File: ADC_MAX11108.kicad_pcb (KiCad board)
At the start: 4 copper layers, 100 x 100 mm, 82 parts, among them IC1 MAX11108AVB+T, IC2 MAX11108AVB+T, IC22 524SDCGI8, IC24 524SDCGI8, IC26 524SDCGI8, IC28 524SDCGI8, IC30 LMS1585ACSX-ADJ_NOPB, J1 Conn_01x02_Pin, J2 Conn_01x03_Pin, J3 Conn_01x07_Pin, J4 Conn_01x07_Pin, J5 Conn_01x07_Pin, J6 Conn_01x08_Pin, J7 Conn_01x08_Pin, Q1 LMS1587CT-3.3_NOPB, U1 ADR4533, U2 ADR4533, U3 ADR4533, U4 ADR4533, U5 ADR4533

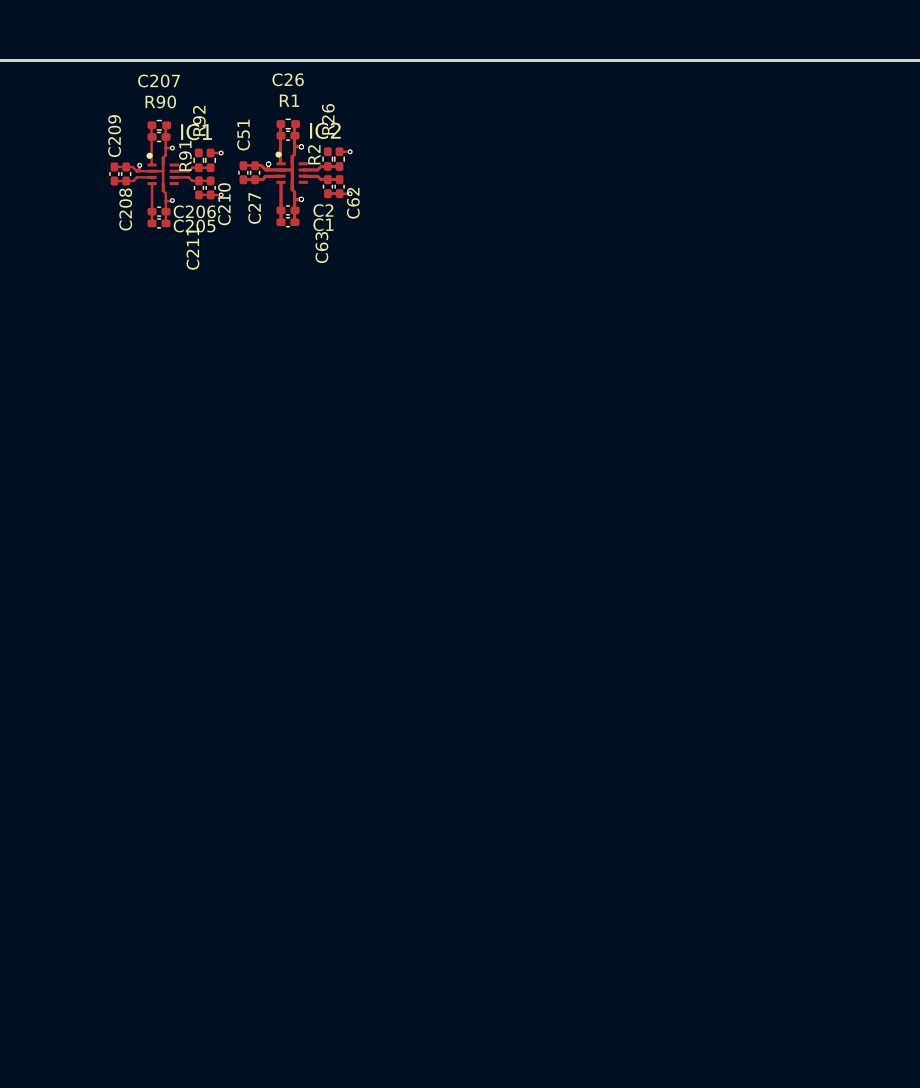
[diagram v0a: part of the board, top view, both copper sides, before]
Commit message: figured out footprint issue and replicated the 25 ADCs in the routing part as well
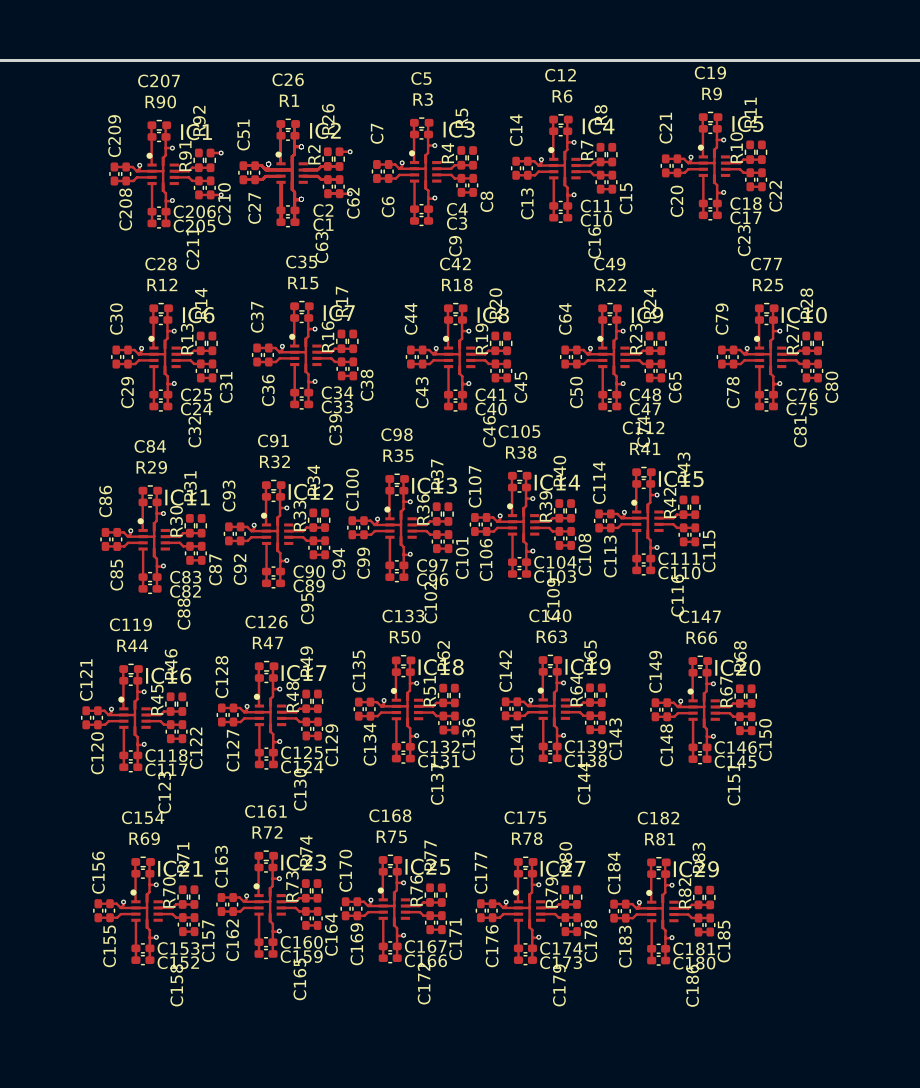
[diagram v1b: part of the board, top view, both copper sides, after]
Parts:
- added C10: 10uF, Capacitor_SMD:C_0402_1005Metric_Pad0.74x0.62mm_HandSolder, F.Cu at (148.7, 61.6)
- added C100: 10uF, Capacitor_SMD:C_0402_1005Metric_Pad0.74x0.62mm_HandSolder, F.Cu at (131.8, 86.8)
- added C101: 10uF, Capacitor_SMD:C_0402_1005Metric_Pad0.74x0.62mm_HandSolder, F.Cu at (139.6, 87.9)
- added C102: 0.1uF, Capacitor_SMD:C_0402_1005Metric_Pad0.74x0.62mm_HandSolder, F.Cu at (138.6, 87.9)
- added C103: 10uF, Capacitor_SMD:C_0402_1005Metric_Pad0.74x0.62mm_HandSolder, F.Cu at (145.3, 90.5)
- added C104: 0.1uF, Capacitor_SMD:C_0402_1005Metric_Pad0.74x0.62mm_HandSolder, F.Cu at (145.3, 89.6)
- added C105: 470pF, Capacitor_SMD:C_0402_1005Metric_Pad0.74x0.62mm_HandSolder, F.Cu at (145.3, 83.5)
- added C106: 0.1uF, Capacitor_SMD:C_0402_1005Metric_Pad0.74x0.62mm_HandSolder, F.Cu at (142.7, 86.5)
- added C107: 10uF, Capacitor_SMD:C_0402_1005Metric_Pad0.74x0.62mm_HandSolder, F.Cu at (141.7, 86.5)
- added C108: 10uF, Capacitor_SMD:C_0402_1005Metric_Pad0.74x0.62mm_HandSolder, F.Cu at (149.5, 87.6)
- added C109: 0.1uF, Capacitor_SMD:C_0402_1005Metric_Pad0.74x0.62mm_HandSolder, F.Cu at (148.6, 87.6)
- added C11: 0.1uF, Capacitor_SMD:C_0402_1005Metric_Pad0.74x0.62mm_HandSolder, F.Cu at (148.7, 60.7)
- added C110: 10uF, Capacitor_SMD:C_0402_1005Metric_Pad0.74x0.62mm_HandSolder, F.Cu at (155.4, 90.2)
- added C111: 0.1uF, Capacitor_SMD:C_0402_1005Metric_Pad0.74x0.62mm_HandSolder, F.Cu at (155.4, 89.3)
- added C112: 470pF, Capacitor_SMD:C_0402_1005Metric_Pad0.74x0.62mm_HandSolder, F.Cu at (155.4, 83.2)
- added C113: 0.1uF, Capacitor_SMD:C_0402_1005Metric_Pad0.74x0.62mm_HandSolder, F.Cu at (152.7, 86.2)
- added C114: 10uF, Capacitor_SMD:C_0402_1005Metric_Pad0.74x0.62mm_HandSolder, F.Cu at (151.8, 86.2)
- added C115: 10uF, Capacitor_SMD:C_0402_1005Metric_Pad0.74x0.62mm_HandSolder, F.Cu at (159.6, 87.3)
- added C116: 0.1uF, Capacitor_SMD:C_0402_1005Metric_Pad0.74x0.62mm_HandSolder, F.Cu at (158.6, 87.3)
- added C117: 10uF, Capacitor_SMD:C_0402_1005Metric_Pad0.74x0.62mm_HandSolder, F.Cu at (113.8, 106.2)
- added C118: 0.1uF, Capacitor_SMD:C_0402_1005Metric_Pad0.74x0.62mm_HandSolder, F.Cu at (113.8, 105.2)
- added C119: 470pF, Capacitor_SMD:C_0402_1005Metric_Pad0.74x0.62mm_HandSolder, F.Cu at (113.8, 99.2)
- added C12: 470pF, Capacitor_SMD:C_0402_1005Metric_Pad0.74x0.62mm_HandSolder, F.Cu at (148.7, 54.6)
- added C120: 0.1uF, Capacitor_SMD:C_0402_1005Metric_Pad0.74x0.62mm_HandSolder, F.Cu at (111.2, 102.2)
- added C121: 10uF, Capacitor_SMD:C_0402_1005Metric_Pad0.74x0.62mm_HandSolder, F.Cu at (110.2, 102.2)
- added C122: 10uF, Capacitor_SMD:C_0402_1005Metric_Pad0.74x0.62mm_HandSolder, F.Cu at (118.0, 103.3)
- added C123: 0.1uF, Capacitor_SMD:C_0402_1005Metric_Pad0.74x0.62mm_HandSolder, F.Cu at (117.1, 103.3)
- added C124: 10uF, Capacitor_SMD:C_0402_1005Metric_Pad0.74x0.62mm_HandSolder, F.Cu at (124.8, 105.9)
- added C125: 0.1uF, Capacitor_SMD:C_0402_1005Metric_Pad0.74x0.62mm_HandSolder, F.Cu at (124.8, 105.0)
- added C126: 470pF, Capacitor_SMD:C_0402_1005Metric_Pad0.74x0.62mm_HandSolder, F.Cu at (124.8, 98.9)
- added C127: 0.1uF, Capacitor_SMD:C_0402_1005Metric_Pad0.74x0.62mm_HandSolder, F.Cu at (122.2, 101.9)
- added C128: 10uF, Capacitor_SMD:C_0402_1005Metric_Pad0.74x0.62mm_HandSolder, F.Cu at (121.2, 101.9)
- added C129: 10uF, Capacitor_SMD:C_0402_1005Metric_Pad0.74x0.62mm_HandSolder, F.Cu at (129.0, 103.1)
- added C13: 0.1uF, Capacitor_SMD:C_0402_1005Metric_Pad0.74x0.62mm_HandSolder, F.Cu at (146.0, 57.6)
- added C130: 0.1uF, Capacitor_SMD:C_0402_1005Metric_Pad0.74x0.62mm_HandSolder, F.Cu at (128.1, 103.1)
- added C131: 10uF, Capacitor_SMD:C_0402_1005Metric_Pad0.74x0.62mm_HandSolder, F.Cu at (135.9, 105.5)
- added C132: 0.1uF, Capacitor_SMD:C_0402_1005Metric_Pad0.74x0.62mm_HandSolder, F.Cu at (135.9, 104.5)
- added C133: 470pF, Capacitor_SMD:C_0402_1005Metric_Pad0.74x0.62mm_HandSolder, F.Cu at (135.9, 98.5)
- added C134: 0.1uF, Capacitor_SMD:C_0402_1005Metric_Pad0.74x0.62mm_HandSolder, F.Cu at (133.2, 101.5)
- added C135: 10uF, Capacitor_SMD:C_0402_1005Metric_Pad0.74x0.62mm_HandSolder, F.Cu at (132.3, 101.5)
- added C136: 10uF, Capacitor_SMD:C_0402_1005Metric_Pad0.74x0.62mm_HandSolder, F.Cu at (140.1, 102.6)
- added C137: 0.1uF, Capacitor_SMD:C_0402_1005Metric_Pad0.74x0.62mm_HandSolder, F.Cu at (139.2, 102.6)
- added C138: 10uF, Capacitor_SMD:C_0402_1005Metric_Pad0.74x0.62mm_HandSolder, F.Cu at (147.8, 105.4)
- added C139: 0.1uF, Capacitor_SMD:C_0402_1005Metric_Pad0.74x0.62mm_HandSolder, F.Cu at (147.8, 104.5)
- added C14: 10uF, Capacitor_SMD:C_0402_1005Metric_Pad0.74x0.62mm_HandSolder, F.Cu at (145.1, 57.6)
- added C140: 470pF, Capacitor_SMD:C_0402_1005Metric_Pad0.74x0.62mm_HandSolder, F.Cu at (147.8, 98.4)
- added C141: 0.1uF, Capacitor_SMD:C_0402_1005Metric_Pad0.74x0.62mm_HandSolder, F.Cu at (145.2, 101.4)
- added C142: 10uF, Capacitor_SMD:C_0402_1005Metric_Pad0.74x0.62mm_HandSolder, F.Cu at (144.2, 101.4)
- added C143: 10uF, Capacitor_SMD:C_0402_1005Metric_Pad0.74x0.62mm_HandSolder, F.Cu at (152.0, 102.6)
- added C144: 0.1uF, Capacitor_SMD:C_0402_1005Metric_Pad0.74x0.62mm_HandSolder, F.Cu at (151.1, 102.6)
- added C145: 10uF, Capacitor_SMD:C_0402_1005Metric_Pad0.74x0.62mm_HandSolder, F.Cu at (160.0, 105.5)
- added C146: 0.1uF, Capacitor_SMD:C_0402_1005Metric_Pad0.74x0.62mm_HandSolder, F.Cu at (160.0, 104.6)
- added C147: 470pF, Capacitor_SMD:C_0402_1005Metric_Pad0.74x0.62mm_HandSolder, F.Cu at (160.0, 98.5)
- added C148: 0.1uF, Capacitor_SMD:C_0402_1005Metric_Pad0.74x0.62mm_HandSolder, F.Cu at (157.3, 101.5)
- added C149: 10uF, Capacitor_SMD:C_0402_1005Metric_Pad0.74x0.62mm_HandSolder, F.Cu at (156.3, 101.5)
- added C15: 10uF, Capacitor_SMD:C_0402_1005Metric_Pad0.74x0.62mm_HandSolder, F.Cu at (152.8, 58.8)
- added C150: 10uF, Capacitor_SMD:C_0402_1005Metric_Pad0.74x0.62mm_HandSolder, F.Cu at (164.1, 102.6)
- added C151: 0.1uF, Capacitor_SMD:C_0402_1005Metric_Pad0.74x0.62mm_HandSolder, F.Cu at (163.2, 102.6)
- added C152: 10uF, Capacitor_SMD:C_0402_1005Metric_Pad0.74x0.62mm_HandSolder, F.Cu at (114.8, 121.8)
- added C153: 0.1uF, Capacitor_SMD:C_0402_1005Metric_Pad0.74x0.62mm_HandSolder, F.Cu at (114.8, 120.8)
- added C154: 470pF, Capacitor_SMD:C_0402_1005Metric_Pad0.74x0.62mm_HandSolder, F.Cu at (114.8, 114.8)
- added C155: 0.1uF, Capacitor_SMD:C_0402_1005Metric_Pad0.74x0.62mm_HandSolder, F.Cu at (112.1, 117.8)
- added C156: 10uF, Capacitor_SMD:C_0402_1005Metric_Pad0.74x0.62mm_HandSolder, F.Cu at (111.2, 117.8)
- added C157: 10uF, Capacitor_SMD:C_0402_1005Metric_Pad0.74x0.62mm_HandSolder, F.Cu at (119.0, 118.9)
- added C158: 0.1uF, Capacitor_SMD:C_0402_1005Metric_Pad0.74x0.62mm_HandSolder, F.Cu at (118.0, 118.9)
- added C159: 10uF, Capacitor_SMD:C_0402_1005Metric_Pad0.74x0.62mm_HandSolder, F.Cu at (124.8, 121.3)
- added C16: 0.1uF, Capacitor_SMD:C_0402_1005Metric_Pad0.74x0.62mm_HandSolder, F.Cu at (151.9, 58.8)
- added C160: 0.1uF, Capacitor_SMD:C_0402_1005Metric_Pad0.74x0.62mm_HandSolder, F.Cu at (124.8, 120.3)
- added C161: 470pF, Capacitor_SMD:C_0402_1005Metric_Pad0.74x0.62mm_HandSolder, F.Cu at (124.8, 114.3)
- added C162: 0.1uF, Capacitor_SMD:C_0402_1005Metric_Pad0.74x0.62mm_HandSolder, F.Cu at (122.1, 117.3)
- added C163: 10uF, Capacitor_SMD:C_0402_1005Metric_Pad0.74x0.62mm_HandSolder, F.Cu at (121.2, 117.3)
- added C164: 10uF, Capacitor_SMD:C_0402_1005Metric_Pad0.74x0.62mm_HandSolder, F.Cu at (129.0, 118.4)
- added C165: 0.1uF, Capacitor_SMD:C_0402_1005Metric_Pad0.74x0.62mm_HandSolder, F.Cu at (128.0, 118.4)
- added C166: 10uF, Capacitor_SMD:C_0402_1005Metric_Pad0.74x0.62mm_HandSolder, F.Cu at (134.9, 121.6)
- added C167: 0.1uF, Capacitor_SMD:C_0402_1005Metric_Pad0.74x0.62mm_HandSolder, F.Cu at (134.9, 120.7)
- added C168: 470pF, Capacitor_SMD:C_0402_1005Metric_Pad0.74x0.62mm_HandSolder, F.Cu at (134.9, 114.6)
- added C169: 0.1uF, Capacitor_SMD:C_0402_1005Metric_Pad0.74x0.62mm_HandSolder, F.Cu at (132.2, 117.6)
- added C17: 10uF, Capacitor_SMD:C_0402_1005Metric_Pad0.74x0.62mm_HandSolder, F.Cu at (160.8, 61.4)
- added C170: 10uF, Capacitor_SMD:C_0402_1005Metric_Pad0.74x0.62mm_HandSolder, F.Cu at (131.2, 117.6)
- added C171: 10uF, Capacitor_SMD:C_0402_1005Metric_Pad0.74x0.62mm_HandSolder, F.Cu at (139.0, 118.8)
- added C172: 0.1uF, Capacitor_SMD:C_0402_1005Metric_Pad0.74x0.62mm_HandSolder, F.Cu at (138.1, 118.8)
- added C173: 10uF, Capacitor_SMD:C_0402_1005Metric_Pad0.74x0.62mm_HandSolder, F.Cu at (145.8, 121.8)
- added C174: 0.1uF, Capacitor_SMD:C_0402_1005Metric_Pad0.74x0.62mm_HandSolder, F.Cu at (145.8, 120.8)
- added C175: 470pF, Capacitor_SMD:C_0402_1005Metric_Pad0.74x0.62mm_HandSolder, F.Cu at (145.8, 114.8)
- added C176: 0.1uF, Capacitor_SMD:C_0402_1005Metric_Pad0.74x0.62mm_HandSolder, F.Cu at (143.1, 117.8)
- added C177: 10uF, Capacitor_SMD:C_0402_1005Metric_Pad0.74x0.62mm_HandSolder, F.Cu at (142.2, 117.8)
- added C178: 10uF, Capacitor_SMD:C_0402_1005Metric_Pad0.74x0.62mm_HandSolder, F.Cu at (150.0, 118.9)
- added C179: 0.1uF, Capacitor_SMD:C_0402_1005Metric_Pad0.74x0.62mm_HandSolder, F.Cu at (149.0, 118.9)
- added C18: 0.1uF, Capacitor_SMD:C_0402_1005Metric_Pad0.74x0.62mm_HandSolder, F.Cu at (160.8, 60.5)
- added C180: 10uF, Capacitor_SMD:C_0402_1005Metric_Pad0.74x0.62mm_HandSolder, F.Cu at (156.6, 121.8)
- added C181: 0.1uF, Capacitor_SMD:C_0402_1005Metric_Pad0.74x0.62mm_HandSolder, F.Cu at (156.6, 120.9)
- added C182: 470pF, Capacitor_SMD:C_0402_1005Metric_Pad0.74x0.62mm_HandSolder, F.Cu at (156.6, 114.8)
- added C183: 0.1uF, Capacitor_SMD:C_0402_1005Metric_Pad0.74x0.62mm_HandSolder, F.Cu at (153.9, 117.8)
- added C184: 10uF, Capacitor_SMD:C_0402_1005Metric_Pad0.74x0.62mm_HandSolder, F.Cu at (153.0, 117.8)
- added C185: 10uF, Capacitor_SMD:C_0402_1005Metric_Pad0.74x0.62mm_HandSolder, F.Cu at (160.8, 119.0)
- added C186: 0.1uF, Capacitor_SMD:C_0402_1005Metric_Pad0.74x0.62mm_HandSolder, F.Cu at (159.8, 119.0)
- added C19: 470pF, Capacitor_SMD:C_0402_1005Metric_Pad0.74x0.62mm_HandSolder, F.Cu at (160.8, 54.4)
- added C20: 0.1uF, Capacitor_SMD:C_0402_1005Metric_Pad0.74x0.62mm_HandSolder, F.Cu at (158.1, 57.4)
- added C21: 10uF, Capacitor_SMD:C_0402_1005Metric_Pad0.74x0.62mm_HandSolder, F.Cu at (157.2, 57.4)
- added C22: 10uF, Capacitor_SMD:C_0402_1005Metric_Pad0.74x0.62mm_HandSolder, F.Cu at (165.0, 58.6)
- added C23: 0.1uF, Capacitor_SMD:C_0402_1005Metric_Pad0.74x0.62mm_HandSolder, F.Cu at (164.0, 58.6)
- added C24: 10uF, Capacitor_SMD:C_0402_1005Metric_Pad0.74x0.62mm_HandSolder, F.Cu at (116.3, 76.9)
- added C25: 0.1uF, Capacitor_SMD:C_0402_1005Metric_Pad0.74x0.62mm_HandSolder, F.Cu at (116.3, 76.0)
- added C28: 470pF, Capacitor_SMD:C_0402_1005Metric_Pad0.74x0.62mm_HandSolder, F.Cu at (116.3, 69.9)
- added C29: 0.1uF, Capacitor_SMD:C_0402_1005Metric_Pad0.74x0.62mm_HandSolder, F.Cu at (113.6, 72.9)
- added C3: 10uF, Capacitor_SMD:C_0402_1005Metric_Pad0.74x0.62mm_HandSolder, F.Cu at (137.4, 61.9)
- added C30: 10uF, Capacitor_SMD:C_0402_1005Metric_Pad0.74x0.62mm_HandSolder, F.Cu at (112.7, 72.9)
- added C31: 10uF, Capacitor_SMD:C_0402_1005Metric_Pad0.74x0.62mm_HandSolder, F.Cu at (120.5, 74.1)
- added C32: 0.1uF, Capacitor_SMD:C_0402_1005Metric_Pad0.74x0.62mm_HandSolder, F.Cu at (119.5, 74.1)
- added C33: 10uF, Capacitor_SMD:C_0402_1005Metric_Pad0.74x0.62mm_HandSolder, F.Cu at (127.7, 76.8)
- added C34: 0.1uF, Capacitor_SMD:C_0402_1005Metric_Pad0.74x0.62mm_HandSolder, F.Cu at (127.7, 75.8)
- added C35: 470pF, Capacitor_SMD:C_0402_1005Metric_Pad0.74x0.62mm_HandSolder, F.Cu at (127.7, 69.8)
- added C36: 0.1uF, Capacitor_SMD:C_0402_1005Metric_Pad0.74x0.62mm_HandSolder, F.Cu at (125.0, 72.8)
- added C37: 10uF, Capacitor_SMD:C_0402_1005Metric_Pad0.74x0.62mm_HandSolder, F.Cu at (124.1, 72.8)
- added C38: 10uF, Capacitor_SMD:C_0402_1005Metric_Pad0.74x0.62mm_HandSolder, F.Cu at (131.9, 73.9)
- added C39: 0.1uF, Capacitor_SMD:C_0402_1005Metric_Pad0.74x0.62mm_HandSolder, F.Cu at (130.9, 73.9)
- added C4: 0.1uF, Capacitor_SMD:C_0402_1005Metric_Pad0.74x0.62mm_HandSolder, F.Cu at (137.4, 60.9)
- added C40: 10uF, Capacitor_SMD:C_0402_1005Metric_Pad0.74x0.62mm_HandSolder, F.Cu at (140.1, 76.9)
- added C41: 0.1uF, Capacitor_SMD:C_0402_1005Metric_Pad0.74x0.62mm_HandSolder, F.Cu at (140.1, 76.0)
- added C42: 470pF, Capacitor_SMD:C_0402_1005Metric_Pad0.74x0.62mm_HandSolder, F.Cu at (140.1, 69.9)
- added C43: 0.1uF, Capacitor_SMD:C_0402_1005Metric_Pad0.74x0.62mm_HandSolder, F.Cu at (137.5, 72.9)
- added C44: 10uF, Capacitor_SMD:C_0402_1005Metric_Pad0.74x0.62mm_HandSolder, F.Cu at (136.5, 72.9)
- added C45: 10uF, Capacitor_SMD:C_0402_1005Metric_Pad0.74x0.62mm_HandSolder, F.Cu at (144.3, 74.1)
- added C46: 0.1uF, Capacitor_SMD:C_0402_1005Metric_Pad0.74x0.62mm_HandSolder, F.Cu at (143.4, 74.1)
- added C47: 10uF, Capacitor_SMD:C_0402_1005Metric_Pad0.74x0.62mm_HandSolder, F.Cu at (152.6, 76.9)
- added C48: 0.1uF, Capacitor_SMD:C_0402_1005Metric_Pad0.74x0.62mm_HandSolder, F.Cu at (152.6, 76.0)
- added C49: 470pF, Capacitor_SMD:C_0402_1005Metric_Pad0.74x0.62mm_HandSolder, F.Cu at (152.6, 69.9)
- added C5: 470pF, Capacitor_SMD:C_0402_1005Metric_Pad0.74x0.62mm_HandSolder, F.Cu at (137.4, 54.9)
- added C50: 0.1uF, Capacitor_SMD:C_0402_1005Metric_Pad0.74x0.62mm_HandSolder, F.Cu at (150.0, 72.9)
- added C6: 0.1uF, Capacitor_SMD:C_0402_1005Metric_Pad0.74x0.62mm_HandSolder, F.Cu at (134.7, 57.9)
- added C64: 10uF, Capacitor_SMD:C_0402_1005Metric_Pad0.74x0.62mm_HandSolder, F.Cu at (149.0, 72.9)
- added C65: 10uF, Capacitor_SMD:C_0402_1005Metric_Pad0.74x0.62mm_HandSolder, F.Cu at (156.8, 74.1)
- added C7: 10uF, Capacitor_SMD:C_0402_1005Metric_Pad0.74x0.62mm_HandSolder, F.Cu at (133.8, 57.9)
- added C74: 0.1uF, Capacitor_SMD:C_0402_1005Metric_Pad0.74x0.62mm_HandSolder, F.Cu at (155.9, 74.1)
- added C75: 10uF, Capacitor_SMD:C_0402_1005Metric_Pad0.74x0.62mm_HandSolder, F.Cu at (165.3, 76.9)
- added C76: 0.1uF, Capacitor_SMD:C_0402_1005Metric_Pad0.74x0.62mm_HandSolder, F.Cu at (165.3, 76.0)
- added C77: 470pF, Capacitor_SMD:C_0402_1005Metric_Pad0.74x0.62mm_HandSolder, F.Cu at (165.3, 69.9)
- added C78: 0.1uF, Capacitor_SMD:C_0402_1005Metric_Pad0.74x0.62mm_HandSolder, F.Cu at (162.7, 72.9)
- added C79: 10uF, Capacitor_SMD:C_0402_1005Metric_Pad0.74x0.62mm_HandSolder, F.Cu at (161.7, 72.9)
- added C8: 10uF, Capacitor_SMD:C_0402_1005Metric_Pad0.74x0.62mm_HandSolder, F.Cu at (141.6, 59.0)
- added C80: 10uF, Capacitor_SMD:C_0402_1005Metric_Pad0.74x0.62mm_HandSolder, F.Cu at (169.5, 74.1)
- added C81: 0.1uF, Capacitor_SMD:C_0402_1005Metric_Pad0.74x0.62mm_HandSolder, F.Cu at (168.6, 74.1)
- added C82: 10uF, Capacitor_SMD:C_0402_1005Metric_Pad0.74x0.62mm_HandSolder, F.Cu at (115.4, 91.7)
- added C83: 0.1uF, Capacitor_SMD:C_0402_1005Metric_Pad0.74x0.62mm_HandSolder, F.Cu at (115.4, 90.8)
- added C84: 470pF, Capacitor_SMD:C_0402_1005Metric_Pad0.74x0.62mm_HandSolder, F.Cu at (115.4, 84.7)
- added C85: 0.1uF, Capacitor_SMD:C_0402_1005Metric_Pad0.74x0.62mm_HandSolder, F.Cu at (112.7, 87.7)
- added C86: 10uF, Capacitor_SMD:C_0402_1005Metric_Pad0.74x0.62mm_HandSolder, F.Cu at (111.8, 87.7)
- added C87: 10uF, Capacitor_SMD:C_0402_1005Metric_Pad0.74x0.62mm_HandSolder, F.Cu at (119.6, 88.8)
- added C88: 0.1uF, Capacitor_SMD:C_0402_1005Metric_Pad0.74x0.62mm_HandSolder, F.Cu at (118.6, 88.8)
- added C89: 10uF, Capacitor_SMD:C_0402_1005Metric_Pad0.74x0.62mm_HandSolder, F.Cu at (125.4, 91.3)
- added C9: 0.1uF, Capacitor_SMD:C_0402_1005Metric_Pad0.74x0.62mm_HandSolder, F.Cu at (140.6, 59.0)
- added C90: 0.1uF, Capacitor_SMD:C_0402_1005Metric_Pad0.74x0.62mm_HandSolder, F.Cu at (125.4, 90.3)
- added C91: 470pF, Capacitor_SMD:C_0402_1005Metric_Pad0.74x0.62mm_HandSolder, F.Cu at (125.4, 84.3)
- added C92: 0.1uF, Capacitor_SMD:C_0402_1005Metric_Pad0.74x0.62mm_HandSolder, F.Cu at (122.7, 87.3)
- added C93: 10uF, Capacitor_SMD:C_0402_1005Metric_Pad0.74x0.62mm_HandSolder, F.Cu at (121.8, 87.3)
- added C94: 10uF, Capacitor_SMD:C_0402_1005Metric_Pad0.74x0.62mm_HandSolder, F.Cu at (129.6, 88.4)
- added C95: 0.1uF, Capacitor_SMD:C_0402_1005Metric_Pad0.74x0.62mm_HandSolder, F.Cu at (128.6, 88.4)
- added C96: 10uF, Capacitor_SMD:C_0402_1005Metric_Pad0.74x0.62mm_HandSolder, F.Cu at (135.4, 90.8)
- added C97: 0.1uF, Capacitor_SMD:C_0402_1005Metric_Pad0.74x0.62mm_HandSolder, F.Cu at (135.4, 89.8)
- added C98: 470pF, Capacitor_SMD:C_0402_1005Metric_Pad0.74x0.62mm_HandSolder, F.Cu at (135.4, 83.8)
- added C99: 0.1uF, Capacitor_SMD:C_0402_1005Metric_Pad0.74x0.62mm_HandSolder, F.Cu at (132.7, 86.8)
- added IC10: MAX11108AVB+T, My_footprints:QFN50P160X210X50-10N-D, F.Cu at (165.7, 73.0)
- added IC11: MAX11108AVB+T, My_footprints:QFN50P160X210X50-10N-D, F.Cu at (115.7, 87.7)
- added IC12: MAX11108AVB+T, My_footprints:QFN50P160X210X50-10N-D, F.Cu at (125.7, 87.3)
- added IC13: MAX11108AVB+T, My_footprints:QFN50P160X210X50-10N-D, F.Cu at (135.7, 86.8)
- added IC14: MAX11108AVB+T, My_footprints:QFN50P160X210X50-10N-D, F.Cu at (145.7, 86.5)
- added IC15: MAX11108AVB+T, My_footprints:QFN50P160X210X50-10N-D, F.Cu at (155.7, 86.2)
- added IC16: MAX11108AVB+T, My_footprints:QFN50P160X210X50-10N-D, F.Cu at (114.2, 102.2)
- added IC17: MAX11108AVB+T, My_footprints:QFN50P160X210X50-10N-D, F.Cu at (125.2, 102.0)
- added IC18: MAX11108AVB+T, My_footprints:QFN50P160X210X50-10N-D, F.Cu at (136.2, 101.5)
- added IC19: MAX11108AVB+T, My_footprints:QFN50P160X210X50-10N-D, F.Cu at (148.2, 101.5)
- added IC20: MAX11108AVB+T, My_footprints:QFN50P160X210X50-10N-D, F.Cu at (160.3, 101.5)
- added IC21: MAX11108AVB+T, My_footprints:QFN50P160X210X50-10N-D, F.Cu at (115.1, 117.8)
- added IC23: MAX11108AVB+T, My_footprints:QFN50P160X210X50-10N-D, F.Cu at (125.1, 117.3)
- added IC25: MAX11108AVB+T, My_footprints:QFN50P160X210X50-10N-D, F.Cu at (135.2, 117.7)
- added IC27: MAX11108AVB+T, My_footprints:QFN50P160X210X50-10N-D, F.Cu at (146.1, 117.8)
- added IC29: MAX11108AVB+T, My_footprints:QFN50P160X210X50-10N-D, F.Cu at (156.9, 117.9)
- added IC3: MAX11108AVB+T, My_footprints:QFN50P160X210X50-10N-D, F.Cu at (137.7, 57.9)
- added IC4: MAX11108AVB+T, My_footprints:QFN50P160X210X50-10N-D, F.Cu at (149.0, 57.7)
- added IC5: MAX11108AVB+T, My_footprints:QFN50P160X210X50-10N-D, F.Cu at (161.1, 57.5)
- added IC6: MAX11108AVB+T, My_footprints:QFN50P160X210X50-10N-D, F.Cu at (116.6, 73.0)
- added IC7: MAX11108AVB+T, My_footprints:QFN50P160X210X50-10N-D, F.Cu at (128.0, 72.8)
- added IC8: MAX11108AVB+T, My_footprints:QFN50P160X210X50-10N-D, F.Cu at (140.5, 73.0)
- added IC9: MAX11108AVB+T, My_footprints:QFN50P160X210X50-10N-D, F.Cu at (153.0, 73.0)
- added R10: 50K, Resistor_SMD:R_0402_1005Metric_Pad0.72x0.64mm_HandSolder, F.Cu at (165.0, 56.3)
- added R11: ERA-2AKD220X, Resistor_SMD:R_0402_1005Metric_Pad0.72x0.64mm_HandSolder, F.Cu at (164.0, 56.3)
- added R12: ERA-2ARB103X, Resistor_SMD:R_0402_1005Metric_Pad0.72x0.64mm_HandSolder, F.Cu at (116.3, 69.0)
- added R13: 50K, Resistor_SMD:R_0402_1005Metric_Pad0.72x0.64mm_HandSolder, F.Cu at (120.4, 71.8)
- added R14: ERA-2AKD220X, Resistor_SMD:R_0402_1005Metric_Pad0.72x0.64mm_HandSolder, F.Cu at (119.5, 71.8)
- added R15: ERA-2ARB103X, Resistor_SMD:R_0402_1005Metric_Pad0.72x0.64mm_HandSolder, F.Cu at (127.7, 68.8)
- added R16: 50K, Resistor_SMD:R_0402_1005Metric_Pad0.72x0.64mm_HandSolder, F.Cu at (131.8, 71.7)
- added R17: ERA-2AKD220X, Resistor_SMD:R_0402_1005Metric_Pad0.72x0.64mm_HandSolder, F.Cu at (130.9, 71.7)
- added R18: ERA-2ARB103X, Resistor_SMD:R_0402_1005Metric_Pad0.72x0.64mm_HandSolder, F.Cu at (140.2, 69.0)
- added R19: 50K, Resistor_SMD:R_0402_1005Metric_Pad0.72x0.64mm_HandSolder, F.Cu at (144.3, 71.8)
- added R20: ERA-2AKD220X, Resistor_SMD:R_0402_1005Metric_Pad0.72x0.64mm_HandSolder, F.Cu at (143.4, 71.8)
- added R22: ERA-2ARB103X, Resistor_SMD:R_0402_1005Metric_Pad0.72x0.64mm_HandSolder, F.Cu at (152.7, 69.0)
- added R23: 50K, Resistor_SMD:R_0402_1005Metric_Pad0.72x0.64mm_HandSolder, F.Cu at (156.8, 71.8)
- added R24: ERA-2AKD220X, Resistor_SMD:R_0402_1005Metric_Pad0.72x0.64mm_HandSolder, F.Cu at (155.9, 71.8)
- added R25: ERA-2ARB103X, Resistor_SMD:R_0402_1005Metric_Pad0.72x0.64mm_HandSolder, F.Cu at (165.4, 69.0)
- added R27: 50K, Resistor_SMD:R_0402_1005Metric_Pad0.72x0.64mm_HandSolder, F.Cu at (169.5, 71.8)
- added R28: ERA-2AKD220X, Resistor_SMD:R_0402_1005Metric_Pad0.72x0.64mm_HandSolder, F.Cu at (168.6, 71.8)
- added R29: ERA-2ARB103X, Resistor_SMD:R_0402_1005Metric_Pad0.72x0.64mm_HandSolder, F.Cu at (115.4, 83.8)
- added R3: ERA-2ARB103X, Resistor_SMD:R_0402_1005Metric_Pad0.72x0.64mm_HandSolder, F.Cu at (137.4, 53.9)
- added R30: 50K, Resistor_SMD:R_0402_1005Metric_Pad0.72x0.64mm_HandSolder, F.Cu at (119.6, 86.6)
- added R31: ERA-2AKD220X, Resistor_SMD:R_0402_1005Metric_Pad0.72x0.64mm_HandSolder, F.Cu at (118.6, 86.6)
- added R32: ERA-2ARB103X, Resistor_SMD:R_0402_1005Metric_Pad0.72x0.64mm_HandSolder, F.Cu at (125.4, 83.3)
- added R33: 50K, Resistor_SMD:R_0402_1005Metric_Pad0.72x0.64mm_HandSolder, F.Cu at (129.6, 86.2)
- added R34: ERA-2AKD220X, Resistor_SMD:R_0402_1005Metric_Pad0.72x0.64mm_HandSolder, F.Cu at (128.6, 86.2)
- added R35: ERA-2ARB103X, Resistor_SMD:R_0402_1005Metric_Pad0.72x0.64mm_HandSolder, F.Cu at (135.4, 82.8)
- added R36: 50K, Resistor_SMD:R_0402_1005Metric_Pad0.72x0.64mm_HandSolder, F.Cu at (139.6, 85.7)
- added R37: ERA-2AKD220X, Resistor_SMD:R_0402_1005Metric_Pad0.72x0.64mm_HandSolder, F.Cu at (138.6, 85.7)
- added R38: ERA-2ARB103X, Resistor_SMD:R_0402_1005Metric_Pad0.72x0.64mm_HandSolder, F.Cu at (145.3, 82.6)
- added R39: 50K, Resistor_SMD:R_0402_1005Metric_Pad0.72x0.64mm_HandSolder, F.Cu at (149.5, 85.4)
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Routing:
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
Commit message: Updated schematic and PCB layout, no more precision Vrefs
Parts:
- removed C194, C52, C54, C58, C59: 10uF, Capacitor_SMD:C_0402_1005Metric_Pad0.74x0.62mm_HandSolder
- removed C53, C55, C56, C57, C60, C61, C69, C71, C73: 0.1uF, Capacitor_SMD:C_0402_1005Metric_Pad0.74x0.62mm_HandSolder
- removed U1, U2, U3, U4, U5: ADR4533, Package_SO:SOIC-8_3.9x4.9mm_P1.27mm
- added J8: Conn_01x02_Pin, Connector_PinHeader_2.54mm:PinHeader_1x02_P2.54mm_Vertical, F.Cu at (175.0, 97.0)
- C195, C68, C70, C72: value 10uF -> 0.01uF
- C196, C197, C66, C67: value C -> 10uF
- IC22, IC24, IC26, IC28: moved to B.Cu
- J2: value Conn_01x03_Pin -> Conn_01x02_Pin; footprint Connector_PinHeader_2.54mm:PinHeader_1x03_P2.54mm_Vertical -> Connector_PinHeader_2.54mm:PinHeader_1x02_P2.54mm_Vertical
- moved Basys1_connect1 240.8 mm to (103.3, 141.6), turned to 180 degrees
- moved J7 237.0 mm to (110.0, 103.0)
- moved IC26 236.3 mm to (109.5, 54.4)
- moved IC22 233.1 mm to (104.0, 84.3)
- moved IC28 221.0 mm to (119.8, 82.2)
- moved Basys1_connect2 220.6 mm to (119.4, 141.6), turned to 180 degrees
- moved IC24 220.3 mm to (119.5, 74.2)
- moved J5 208.6 mm to (143.2, 85.3), turned to 90 degrees
- moved J4 203.8 mm to (143.2, 71.5), turned to 90 degrees
- moved Basys2_connect1 200.9 mm to (135.4, 141.6), turned to 180 degrees
- moved J6 200.7 mm to (141.9, 99.4), turned to 90 degrees
- moved J3 200.0 mm to (143.2, 57.1), turned to 90 degrees
- moved Basys2_connect2 181.8 mm to (151.4, 141.6), turned to 180 degrees
- moved Barrel_Jack1 164.9 mm to (189.2, 89.2), turned to -90 degrees
- moved Basys_1_Backup1 163.4 mm to (167.5, 141.6), turned to 180 degrees
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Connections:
- C1 pad 1: 3.4V -> 3.3_ADJ
- C10 pad 1: 3.4V -> 3.3_ADJ
- C100 pad 1: V_Ref_3 -> 3.3VRef
- C101 pad 1: +3.3V -> 3.3_ADJ
- C102 pad 1: +3.3V -> 3.3_ADJ
- C103 pad 1: 3.4V -> 3.3_ADJ
- C104 pad 1: 3.4V -> 3.3_ADJ
- C106 pad 1: V_Ref_3 -> 3.3VRef
- C107 pad 1: V_Ref_3 -> 3.3VRef
- C108 pad 1: +3.3V -> 3.3_ADJ
- C109 pad 1: +3.3V -> 3.3_ADJ
- C11 pad 1: 3.4V -> 3.3_ADJ
- C110 pad 1: 3.4V -> 3.3_ADJ
- C111 pad 1: 3.4V -> 3.3_ADJ
- C113 pad 1: V_Ref_3 -> 3.3VRef
- C114 pad 1: V_Ref_3 -> 3.3VRef
- C115 pad 1: +3.3V -> 3.3_ADJ
- C116 pad 1: +3.3V -> 3.3_ADJ
- C117 pad 1: 3.4V -> 3.3_ADJ
- C118 pad 1: 3.4V -> 3.3_ADJ
- C120 pad 1: V_Ref_4 -> 3.3VRef
- C121 pad 1: V_Ref_4 -> 3.3VRef
- C122 pad 1: +3.3V -> 3.3_ADJ
- C123 pad 1: +3.3V -> 3.3_ADJ
- C124 pad 1: 3.4V -> 3.3_ADJ
- C125 pad 1: 3.4V -> 3.3_ADJ
- C127 pad 1: V_Ref_4 -> 3.3VRef
- C128 pad 1: V_Ref_4 -> 3.3VRef
- C129 pad 1: +3.3V -> 3.3_ADJ
- C13 pad 1: V_Ref_1 -> 3.3VRef
- C130 pad 1: +3.3V -> 3.3_ADJ
- C131 pad 1: 3.4V -> 3.3_ADJ
- C132 pad 1: 3.4V -> 3.3_ADJ
- C134 pad 1: V_Ref_4 -> 3.3VRef
- C135 pad 1: V_Ref_4 -> 3.3VRef
- C136 pad 1: +3.3V -> 3.3_ADJ
- C137 pad 1: +3.3V -> 3.3_ADJ
- C138 pad 1: 3.4V -> 3.3_ADJ
- C139 pad 1: 3.4V -> 3.3_ADJ
- C14 pad 1: V_Ref_1 -> 3.3VRef
- C141 pad 1: V_Ref_4 -> 3.3VRef
- C142 pad 1: V_Ref_4 -> 3.3VRef
- C143 pad 1: +3.3V -> 3.3_ADJ
- C144 pad 1: +3.3V -> 3.3_ADJ
- C145 pad 1: 3.4V -> 3.3_ADJ
- C146 pad 1: 3.4V -> 3.3_ADJ
- C148 pad 1: V_Ref_4 -> 3.3VRef
- C149 pad 1: V_Ref_4 -> 3.3VRef
- C15 pad 1: +3.3V -> 3.3_ADJ
- C150 pad 1: +3.3V -> 3.3_ADJ
- C151 pad 1: +3.3V -> 3.3_ADJ
- C152 pad 1: 3.4V -> 3.3_ADJ
- C153 pad 1: 3.4V -> 3.3_ADJ
- C155 pad 1: V_Ref_5 -> 3.3VRef
- C156 pad 1: V_Ref_5 -> 3.3VRef
- C157 pad 1: +3.3V -> 3.3_ADJ
- C158 pad 1: +3.3V -> 3.3_ADJ
- C159 pad 1: 3.4V -> 3.3_ADJ
- C16 pad 1: +3.3V -> 3.3_ADJ
- C160 pad 1: 3.4V -> 3.3_ADJ
- C162 pad 1: V_Ref_5 -> 3.3VRef
- C163 pad 1: V_Ref_5 -> 3.3VRef
- C164 pad 1: +3.3V -> 3.3_ADJ
- C165 pad 1: +3.3V -> 3.3_ADJ
- C166 pad 1: 3.4V -> 3.3_ADJ
- C167 pad 1: 3.4V -> 3.3_ADJ
- C169 pad 1: V_Ref_5 -> 3.3VRef
- C17 pad 1: 3.4V -> 3.3_ADJ
- C170 pad 1: V_Ref_5 -> 3.3VRef
- C171 pad 1: +3.3V -> 3.3_ADJ
- C172 pad 1: +3.3V -> 3.3_ADJ
- C173 pad 1: 3.4V -> 3.3_ADJ
- C174 pad 1: 3.4V -> 3.3_ADJ
- C176 pad 1: V_Ref_5 -> 3.3VRef
- C177 pad 1: V_Ref_5 -> 3.3VRef
- C178 pad 1: +3.3V -> 3.3_ADJ
- C179 pad 1: +3.3V -> 3.3_ADJ
- C18 pad 1: 3.4V -> 3.3_ADJ
- C180 pad 1: 3.4V -> 3.3_ADJ
- C181 pad 1: 3.4V -> 3.3_ADJ
- C183 pad 1: V_Ref_5 -> 3.3VRef
- C184 pad 1: V_Ref_5 -> 3.3VRef
- C185 pad 1: +3.3V -> 3.3_ADJ
- C186 pad 1: +3.3V -> 3.3_ADJ
- C195 pad 1: +3.3V -> 3.3_ADJ
- C196 pad 1: unconnected-(C196-Pad1) -> Net-(IC30-OUTPUT)
- C196 pad 2: unconnected-(C196-Pad2) -> GND
- C197 pad 1: unconnected-(C197-Pad1) -> Switch_out
- C197 pad 2: unconnected-(C197-Pad2) -> GND
- C2 pad 1: 3.4V -> 3.3_ADJ
- C20 pad 1: V_Ref_1 -> 3.3VRef
- C205 pad 1: 3.4V -> 3.3_ADJ
- C206 pad 1: 3.4V -> 3.3_ADJ
- C208 pad 1: V_Ref_1 -> 3.3VRef
- C209 pad 1: V_Ref_1 -> 3.3VRef
- C21 pad 1: V_Ref_1 -> 3.3VRef
- C210 pad 1: +3.3V -> 3.3_ADJ
- C211 pad 1: +3.3V -> 3.3_ADJ
- C22 pad 1: +3.3V -> 3.3_ADJ
- C23 pad 1: +3.3V -> 3.3_ADJ
- C24 pad 1: 3.4V -> 3.3_ADJ
- C25 pad 1: 3.4V -> 3.3_ADJ
- C27 pad 1: V_Ref_1 -> 3.3VRef
- C29 pad 1: V_Ref_2 -> 3.3VRef
- C3 pad 1: 3.4V -> 3.3_ADJ
- C30 pad 1: V_Ref_2 -> 3.3VRef
- C31 pad 1: +3.3V -> 3.3_ADJ
- C32 pad 1: +3.3V -> 3.3_ADJ
- C33 pad 1: 3.4V -> 3.3_ADJ
- C34 pad 1: 3.4V -> 3.3_ADJ
- C36 pad 1: V_Ref_2 -> 3.3VRef
- C37 pad 1: V_Ref_2 -> 3.3VRef
- C38 pad 1: +3.3V -> 3.3_ADJ
- C39 pad 1: +3.3V -> 3.3_ADJ
- C4 pad 1: 3.4V -> 3.3_ADJ
- C40 pad 1: 3.4V -> 3.3_ADJ
- C41 pad 1: 3.4V -> 3.3_ADJ
- C43 pad 1: V_Ref_2 -> 3.3VRef
- C44 pad 1: V_Ref_2 -> 3.3VRef
- C45 pad 1: +3.3V -> 3.3_ADJ
- C46 pad 1: +3.3V -> 3.3_ADJ
- C47 pad 1: 3.4V -> 3.3_ADJ
- C48 pad 1: 3.4V -> 3.3_ADJ
- C50 pad 1: V_Ref_2 -> 3.3VRef
- C51 pad 1: V_Ref_1 -> 3.3VRef
- C6 pad 1: V_Ref_1 -> 3.3VRef
- C62 pad 1: +3.3V -> 3.3_ADJ
- C63 pad 1: +3.3V -> 3.3_ADJ
- C64 pad 1: V_Ref_2 -> 3.3VRef
- C65 pad 1: +3.3V -> 3.3_ADJ
- C66 pad 1: unconnected-(C66-Pad1) -> Vref_LDO
- C66 pad 2: unconnected-(C66-Pad2) -> GND
- C67 pad 1: unconnected-(C67-Pad1) -> GND
- C67 pad 2: unconnected-(C67-Pad2) -> Switch_out
- C68 pad 1: +3.3V -> 3.3_ADJ
- C7 pad 1: V_Ref_1 -> 3.3VRef
- C70 pad 1: +3.3V -> 3.3_ADJ
- C72 pad 1: +3.3V -> 3.3_ADJ
- C74 pad 1: +3.3V -> 3.3_ADJ
- C75 pad 1: 3.4V -> 3.3_ADJ
- C76 pad 1: 3.4V -> 3.3_ADJ
- C78 pad 1: V_Ref_2 -> 3.3VRef
- C79 pad 1: V_Ref_2 -> 3.3VRef
- C8 pad 1: +3.3V -> 3.3_ADJ
- C80 pad 1: +3.3V -> 3.3_ADJ
- C81 pad 1: +3.3V -> 3.3_ADJ
- C82 pad 1: 3.4V -> 3.3_ADJ
- C83 pad 1: 3.4V -> 3.3_ADJ
- C85 pad 1: V_Ref_3 -> 3.3VRef
- C86 pad 1: V_Ref_3 -> 3.3VRef
- C87 pad 1: +3.3V -> 3.3_ADJ
- C88 pad 1: +3.3V -> 3.3_ADJ
- C89 pad 1: 3.4V -> 3.3_ADJ
- C9 pad 1: +3.3V -> 3.3_ADJ
- C90 pad 1: 3.4V -> 3.3_ADJ
- C92 pad 1: V_Ref_3 -> 3.3VRef
- C93 pad 1: V_Ref_3 -> 3.3VRef
- C94 pad 1: +3.3V -> 3.3_ADJ
- C95 pad 1: +3.3V -> 3.3_ADJ
- C96 pad 1: 3.4V -> 3.3_ADJ
- C97 pad 1: 3.4V -> 3.3_ADJ
- C99 pad 1: V_Ref_3 -> 3.3VRef
- IC1 pad 3: V_Ref_1 -> 3.3VRef
- IC1 pad 4: 3.4V -> 3.3_ADJ
- IC1 pad 7: +3.3V -> 3.3_ADJ
- IC10 pad 3: V_Ref_2 -> 3.3VRef
- IC10 pad 4: 3.4V -> 3.3_ADJ
- IC10 pad 7: +3.3V -> 3.3_ADJ
- IC11 pad 3: V_Ref_3 -> 3.3VRef
- IC11 pad 4: 3.4V -> 3.3_ADJ
- IC11 pad 7: +3.3V -> 3.3_ADJ
- IC12 pad 3: V_Ref_3 -> 3.3VRef
- IC12 pad 4: 3.4V -> 3.3_ADJ
- IC12 pad 7: +3.3V -> 3.3_ADJ
- IC13 pad 3: V_Ref_3 -> 3.3VRef
- IC13 pad 4: 3.4V -> 3.3_ADJ
- IC13 pad 7: +3.3V -> 3.3_ADJ
- IC14 pad 3: V_Ref_3 -> 3.3VRef
- IC14 pad 4: 3.4V -> 3.3_ADJ
- IC14 pad 7: +3.3V -> 3.3_ADJ
- IC15 pad 3: V_Ref_3 -> 3.3VRef
- IC15 pad 4: 3.4V -> 3.3_ADJ
- IC15 pad 7: +3.3V -> 3.3_ADJ
- IC16 pad 3: V_Ref_4 -> 3.3VRef
- IC16 pad 4: 3.4V -> 3.3_ADJ
- IC16 pad 7: +3.3V -> 3.3_ADJ
- IC17 pad 3: V_Ref_4 -> 3.3VRef
- IC17 pad 4: 3.4V -> 3.3_ADJ
- IC17 pad 7: +3.3V -> 3.3_ADJ
- IC18 pad 3: V_Ref_4 -> 3.3VRef
- IC18 pad 4: 3.4V -> 3.3_ADJ
- IC18 pad 7: +3.3V -> 3.3_ADJ
- IC19 pad 3: V_Ref_4 -> 3.3VRef
- IC19 pad 4: 3.4V -> 3.3_ADJ
- IC19 pad 7: +3.3V -> 3.3_ADJ
- IC2 pad 3: V_Ref_1 -> 3.3VRef
- IC2 pad 4: 3.4V -> 3.3_ADJ
- IC2 pad 7: +3.3V -> 3.3_ADJ
- IC20 pad 3: V_Ref_4 -> 3.3VRef
- IC20 pad 4: 3.4V -> 3.3_ADJ
- IC20 pad 7: +3.3V -> 3.3_ADJ
- IC21 pad 3: V_Ref_5 -> 3.3VRef
- IC21 pad 4: 3.4V -> 3.3_ADJ
- IC21 pad 7: +3.3V -> 3.3_ADJ
- IC22 pad 5: +3.3V -> 3.3_ADJ
- IC23 pad 3: V_Ref_5 -> 3.3VRef
- IC23 pad 4: 3.4V -> 3.3_ADJ
- IC23 pad 7: +3.3V -> 3.3_ADJ
- IC24 pad 5: +3.3V -> 3.3_ADJ
- IC25 pad 3: V_Ref_5 -> 3.3VRef
- IC25 pad 4: 3.4V -> 3.3_ADJ
- IC25 pad 7: +3.3V -> 3.3_ADJ
- IC26 pad 5: +3.3V -> 3.3_ADJ
- IC27 pad 3: V_Ref_5 -> 3.3VRef
- IC27 pad 4: 3.4V -> 3.3_ADJ
- IC27 pad 7: +3.3V -> 3.3_ADJ
- IC28 pad 5: +3.3V -> 3.3_ADJ
- IC29 pad 3: V_Ref_5 -> 3.3VRef
- IC29 pad 4: 3.4V -> 3.3_ADJ
- IC29 pad 7: +3.3V -> 3.3_ADJ
- IC3 pad 3: V_Ref_1 -> 3.3VRef
- IC3 pad 4: 3.4V -> 3.3_ADJ
- IC3 pad 7: +3.3V -> 3.3_ADJ
- IC4 pad 3: V_Ref_1 -> 3.3VRef
- IC4 pad 4: 3.4V -> 3.3_ADJ
- IC4 pad 7: +3.3V -> 3.3_ADJ
- IC5 pad 3: V_Ref_1 -> 3.3VRef
- IC5 pad 4: 3.4V -> 3.3_ADJ
- IC5 pad 7: +3.3V -> 3.3_ADJ
- IC6 pad 3: V_Ref_2 -> 3.3VRef
- IC6 pad 4: 3.4V -> 3.3_ADJ
- IC6 pad 7: +3.3V -> 3.3_ADJ
- IC7 pad 3: V_Ref_2 -> 3.3VRef
- IC7 pad 4: 3.4V -> 3.3_ADJ
- IC7 pad 7: +3.3V -> 3.3_ADJ
- IC8 pad 3: V_Ref_2 -> 3.3VRef
- IC8 pad 4: 3.4V -> 3.3_ADJ
- IC8 pad 7: +3.3V -> 3.3_ADJ
- IC9 pad 3: V_Ref_2 -> 3.3VRef
- IC9 pad 4: 3.4V -> 3.3_ADJ
- IC9 pad 7: +3.3V -> 3.3_ADJ
- J1 pad 1: 3.4V -> 3.3_ADJ
- J2 pad 2: +3.3V -> Basys_3.3V
- J3 pad 7: +3.3V -> 3.3_ADJ
- J4 pad 7: +3.3V -> 3.3_ADJ
- J5 pad 7: +3.3V -> 3.3_ADJ
- J6 pad 8: +3.3V -> 3.3_ADJ
- Q1 pad 2: Battery_3.3V -> Vref_LDO
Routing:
- net 3.3VRef: track 0.00 -> 549.3 mm
- net GND: track 419.9 -> 746.0 mm, vias 88 -> 185
- net 3.3_ADJ: track 0.00 -> 283.8 mm
- net 3.4V: track 90.7 -> 0.00 mm
- net +3.3V: track 85.9 -> 0.00 mm
- net Ain_12: track 3.24 -> 61.8 mm, vias 0 -> 1
- net Ain_6: track 3.24 -> 43.4 mm, vias 0 -> 1
- net Ain_11: track 3.24 -> 38.4 mm, vias 0 -> 1
- net Ain_16: track 3.24 -> 36.8 mm, vias 0 -> 1
- net Ain_21: track 3.24 -> 33.7 mm, vias 0 -> 1
- net Ain_17: track 3.24 -> 30.9 mm, vias 0 -> 1
- net Ain_20: track 3.24 -> 30.4 mm
- net V_Ref_1: track 25.4 -> 0.00 mm
- net Ain_18: track 3.24 -> 28.2 mm, vias 0 -> 1
- net Ain_22: track 3.24 -> 27.9 mm, vias 0 -> 1
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- removed copper zone on In1.Cu, net (none)
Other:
- board text added: "A 33 OHM series terminating resistor may be used on each clock output if the trace is longer than 1 inch for clk buff"

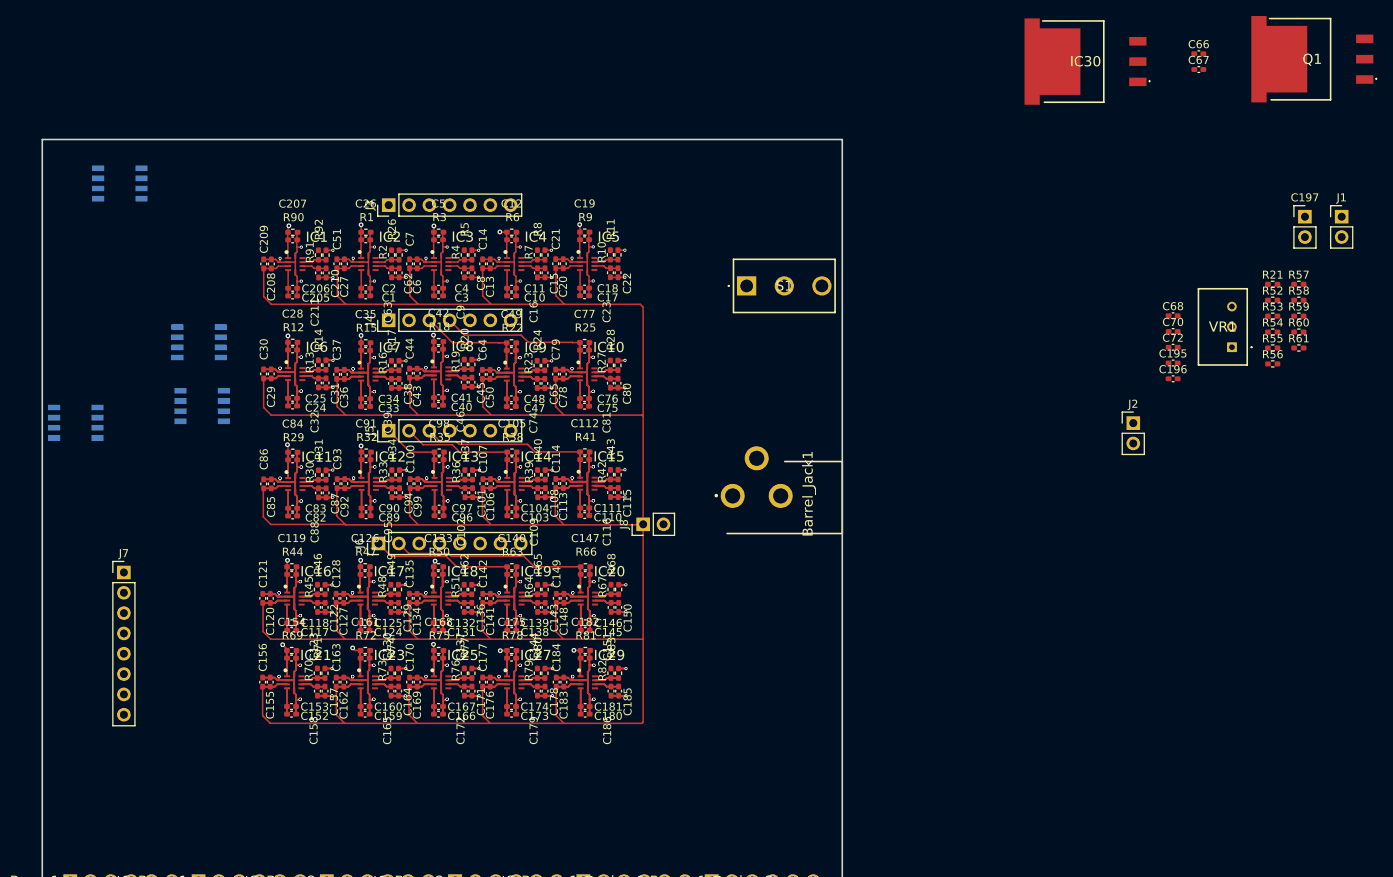
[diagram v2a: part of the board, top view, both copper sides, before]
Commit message: arranged the rest of the parts onto the board
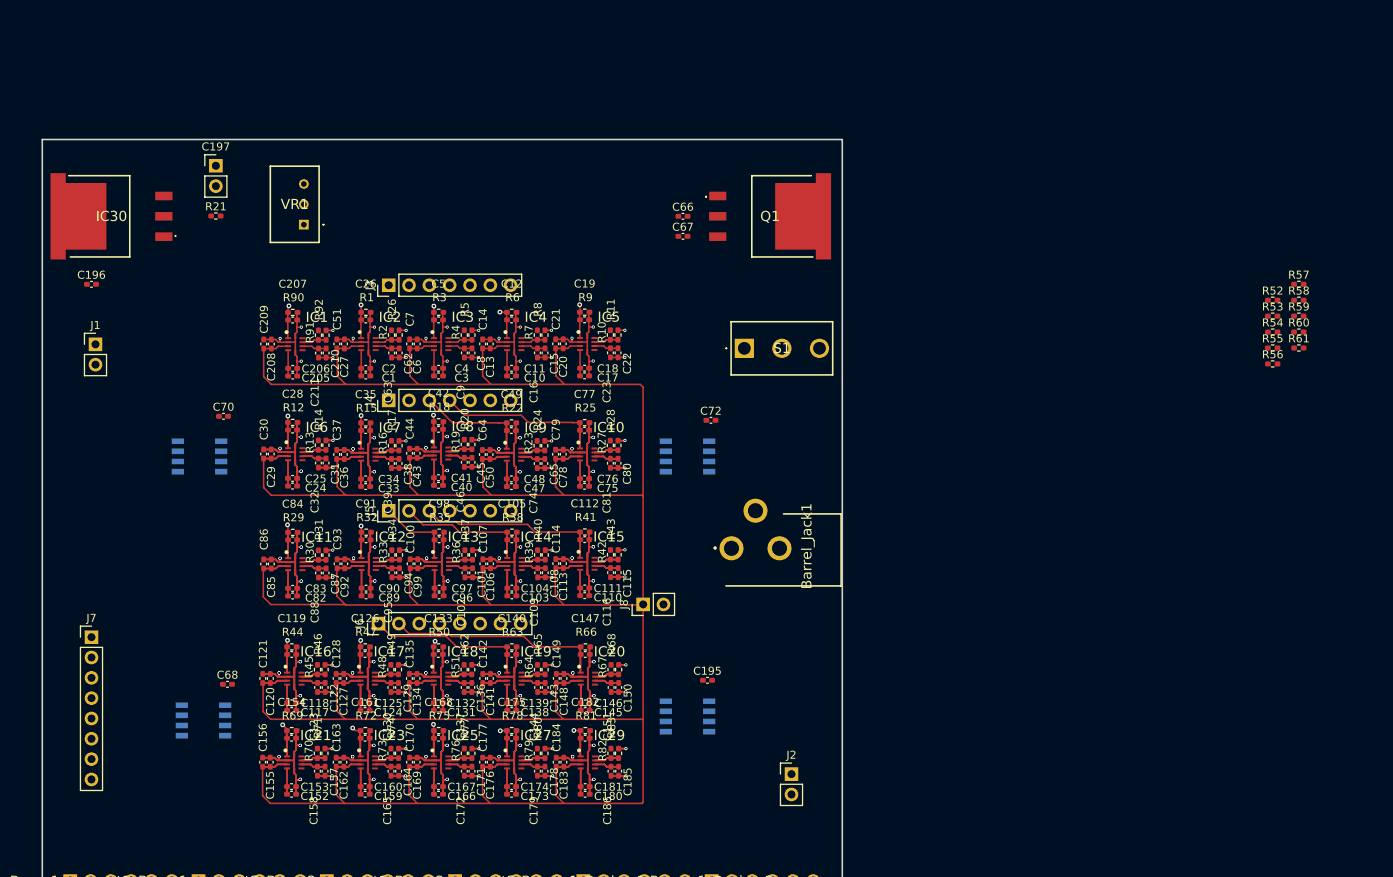
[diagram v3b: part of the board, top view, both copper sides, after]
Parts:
- moved J1 156.6 mm to (106.5, 74.5)
- moved C197 136.3 mm to (121.5, 52.2)
- moved C196 135.7 mm to (106.0, 67.0)
- moved R21 132.4 mm to (121.5, 58.5)
- moved C68 126.9 mm to (123.0, 117.0)
- moved IC30 123.3 mm to (108.5, 58.5)
- moved C70 119.2 mm to (122.5, 83.5)
- moved VR1 117.0 mm to (132.5, 59.5)
- moved IC26 97.3 mm to (180.5, 121.0)
- moved Q1 70.6 mm to (190.8, 58.5), turned to 180 degrees
- moved C195 70.4 mm to (183.0, 116.5)
- moved C67 67.8 mm to (179.9, 61.0)
- moved C66 67.6 mm to (179.9, 58.5)
- moved IC24 62.7 mm to (180.5, 88.5)
- moved J2 61.2 mm to (193.5, 128.2)
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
